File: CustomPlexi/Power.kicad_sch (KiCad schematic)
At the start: 1 part, among them U1 TL074

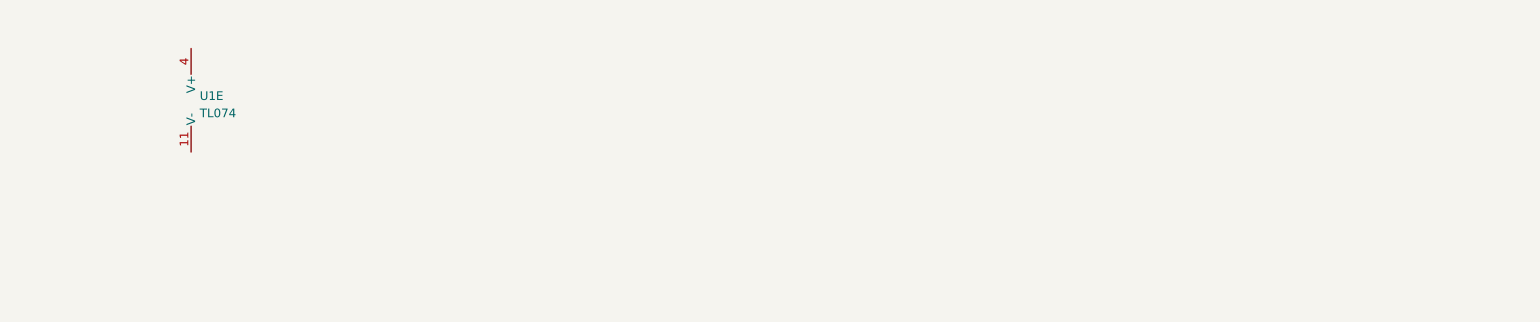
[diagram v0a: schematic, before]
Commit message: input dcdc and negative voltage converter. To decide values
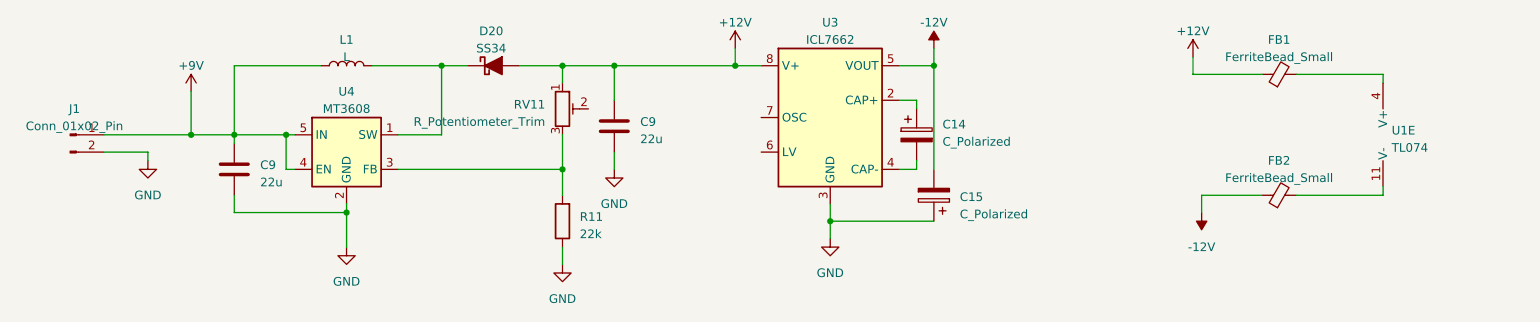
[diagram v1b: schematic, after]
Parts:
- added C14, C15: C_Polarized, symbol Device:C_Polarized
- added C9 (x2): 22u, Capacitor_SMD_AKL:C_0603_1608Metric, symbol PCM_Capacitor_AKL:C_0603
- added D20: SS34, Diode_SMD_AKL:D_SMC, symbol PCM_Diode_Schottky_AKL:SS34
- added FB1, FB2: FerriteBead_Small, symbol Device:FerriteBead_Small
- added J1: Conn_01x02_Pin, symbol Connector:Conn_01x02_Pin
- added L1: L, symbol Device:L
- added R11: 22k, Resistor_SMD_AKL:R_0603_1608Metric, symbol PCM_Resistor_AKL:R_0603
- added RV11: R_Potentiometer_Trim, symbol Device:R_Potentiometer_Trim
- added U3: ICL7662, symbol Regulator_SwitchedCapacitor:ICL7660
- added U4: MT3608, Package_TO_SOT_SMD:SOT-23-6, symbol Regulator_Switching:MT3608
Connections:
- net at U1.11 (V-): now also FB2.2
- net at U1.4 (V+): now also FB1.2
- new net: C14.1, U3.2 (CAP+)
- new net: C14.2, U3.4 (CAP-)
- new net: R11.2, RV11.3, U4.3 (FB)
- new net: D20.1 (K), L1.2, U4.1 (SW)
- new net +12V: C9.2, D20.2 (A), FB1.1, RV11.1, U3.8 (V+)
- new net +9V: C9.2, J1.1 (Pin_1), L1.1, U4.4 (EN), U4.5 (IN)
- new net -12V: C15.2, FB2.1, U3.5 (VOUT)
- new net GND: C15.1, C9.1, C9.1, J1.2 (Pin_2), R11.1, U3.3 (GND), U4.2 (GND)
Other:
- moved on the sheet: U1E

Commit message: commit
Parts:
- C14, C15: footprint (none) -> Capacitor_THT:CP_Radial_D6.3mm_P2.50mm
- C9: footprint Capacitor_SMD_AKL:C_0603_1608Metric -> Capacitor_SMD:C_0402_1005Metric_Pad0.74x0.62mm_HandSolder
- D20: footprint Diode_SMD_AKL:D_SMC -> Diode_SMD:D_0201_0603Metric_Pad0.64x0.40mm_HandSolder
- FB1, FB2: footprint (none) -> PCM_Ferrite_SMD_AKL:Ferrite_0402_1005Metric
- J1: footprint (none) -> Connector_PinHeader_2.54mm:PinHeader_1x02_P2.54mm_Vertical
- L1: footprint (none) -> Inductor_SMD:L_0603_1608Metric
- R11: footprint Resistor_SMD_AKL:R_0603_1608Metric -> Resistor_SMD:R_0402_1005Metric_Pad0.72x0.64mm_HandSolder
- RV11: footprint (none) -> Potentiometer_THT:Potentiometer_Runtron_RM-065_Vertical
- U1: footprint (none) -> Package_SO:SOIC-14W_7.5x9mm_P1.27mm
- U3: footprint (none) -> PCM_Package_SO_AKL:SOIC-8_3.9x4.9mm_P1.27mm
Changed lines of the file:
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@@
       (effects (font (size 1.27 1.27)) (justify right))
     )
-    (property "Footprint" "Capacitor_SMD_AKL:C_0603_1608Metric" (at 52.3748 52.07 0)
+    (property "Footprint" "Capacitor_SMD:C_0402_1005Metric_Pad0.74x0.62mm_HandSolder" (at 52.3748 52.07 0)
       (effects (font (size 1.27 1.27)) hide)
     )
@@
       (effects (font (size 1.27 1.27)) (justify left))
     )
-    (property "Footprint" "" (at 223.52 48.26 0)
+    (property "Footprint" "Package_SO:SOIC-14W_7.5x9mm_P1.27mm" (at 223.52 48.26 0)
       (effects (font (size 1.27 1.27)) hide)
     )
@@
       (effects (font (size 1.27 1.27)))
     )
-    (property "Footprint" "" (at 143.51 50.8 0)
+    (property "Footprint" "PCM_Package_SO_AKL:SOIC-8_3.9x4.9mm_P1.27mm" (at 143.51 50.8 0)
       (effects (font (size 1.27 1.27)) hide)
     )
@@
       (effects (font (size 1.27 1.27)))
     )
-    (property "Footprint" "" (at 207.01 61.468 90)
+    (property "Footprint" "PCM_Ferrite_SMD_AKL:Ferrite_0402_1005Metric" (at 207.01 61.468 90)
       (effects (font (size 1.27 1.27)) hide)
     )
@@
       (effects (font (size 1.27 1.27)) (justify right))
     )
-    (property "Footprint" "Resistor_SMD_AKL:R_0603_1608Metric" (at 101.6 52.07 0)
+    (property "Footprint" "Resistor_SMD:R_0402_1005Metric_Pad0.72x0.64mm_HandSolder" (at 101.6 52.07 0)
       (effects (font (size 1.27 1.27)) hide)
     )
@@
       (effects (font (size 1.27 1.27)))
     )
-    (property "Footprint" "Diode_SMD_AKL:D_SMC" (at 91.44 40.64 0)
+    (property "Footprint" "Diode_SMD:D_0201_0603Metric_Pad0.64x0.40mm_HandSolder" (at 91.44 40.64 0)
       (effects (font (size 1.27 1.27)) hide)
     )
@@
       (effects (font (size 1.27 1.27)) (justify right))
     )
-    (property "Footprint" "Capacitor_SMD_AKL:C_0603_1608Metric" (at 108.2548 45.72 0)
+    (property "Footprint" "Capacitor_SMD:C_0402_1005Metric_Pad0.74x0.62mm_HandSolder" (at 108.2548 45.72 0)
       (effects (font (size 1.27 1.27)) hide)
     )
@@
       (effects (font (size 1.27 1.27)))
     )
-    (property "Footprint" "" (at 29.21 50.8 0)
+    (property "Footprint" "Connector_PinHeader_2.54mm:PinHeader_1x02_P2.54mm_Vertical" (at 29.21 50.8 0)
       (effects (font (size 1.27 1.27)) hide)
     )
@@
       (effects (font (size 1.27 1.27)) (justify right))
     )
-    (property "Footprint" "" (at 101.6 46.99 0)
+    (property "Footprint" "Potentiometer_THT:Potentiometer_Runtron_RM-065_Vertical" (at 101.6 46.99 0)
       (effects (font (size 1.27 1.27)) hide)
     )
@@
       (effects (font (size 1.27 1.27)) (justify left))
     )
-    (property "Footprint" "" (at 154.6352 54.61 0)
+    (property "Footprint" "Capacitor_THT:CP_Radial_D6.3mm_P2.50mm" (at 154.6352 54.61 0)
       (effects (font (size 1.27 1.27)) hide)
     )
@@
       (effects (font (size 1.27 1.27)))
     )
-    (property "Footprint" "" (at 69.85 40.64 0)
+    (property "Footprint" "Inductor_SMD:L_0603_1608Metric" (at 69.85 40.64 0)
       (effects (font (size 1.27 1.27)) hide)
     )
@@
       (effects (font (size 1.27 1.27)))
     )
-    (property "Footprint" "" (at 207.01 43.688 90)
+    (property "Footprint" "PCM_Ferrite_SMD_AKL:Ferrite_0402_1005Metric" (at 207.01 43.688 90)
       (effects (font (size 1.27 1.27)) hide)
     )
@@
       (effects (font (size 1.27 1.27)) (justify right))
     )
-    (property "Footprint" "" (at 155.2448 55.88 0)
-      (effects (font (size 1.27 1.27)) hide)
-    )
+    (property "Footprint" "Capacitor_THT:CP_Radial_D6.3mm_P2.50mm" (at 155.2448 55.88 0)
+      (effects (font (size 1.27 1.27)) hide)
+    )

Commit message: Full ts808
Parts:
- added U5: RC4558, symbol Amplifier_Operational:RC4558
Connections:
- net at FB2.2, U1.11 (V-): now also U5.4 (V-)
- net at FB1.2, U1.4 (V+): now also U5.8 (V+)
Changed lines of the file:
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@@
   (junction (at 60.96 50.8) (diameter 0) (color 0 0 0 0)
   )
+  (junction (at 222.25 59.69) (diameter 0) (color 0 0 0 0)
+  )
   (junction (at 46.99 50.8) (diameter 0) (color 0 0 0 0)
   )
@@
   (junction (at 83.82 40.64) (diameter 0) (color 0 0 0 0)
   )
+  (junction (at 222.25 41.91) (diameter 0) (color 0 0 0 0)
+  )
   (junction (at 156.21 40.64) (diameter 0) (color 0 0 0 0)
   )
@@
     (stroke (width 0) (type default))
   )
+  (wire (pts (xy 233.68 41.91) (xy 222.25 41.91))
+    (stroke (width 0) (type default))
+  )
   (wire (pts (xy 109.22 53.34) (xy 109.22 55.88))
     (stroke (width 0) (type default))
   )
+  (wire (pts (xy 233.68 43.18) (xy 233.68 41.91))
+    (stroke (width 0) (type default))
+  )
   (wire (pts (xy 101.6 55.88) (xy 101.6 59.69))
     (stroke (width 0) (type default))
@@
     (stroke (width 0) (type default))
   )
+  (wire (pts (xy 233.68 59.69) (xy 222.25 59.69))
+    (stroke (width 0) (type default))
+  )
   (wire (pts (xy 222.25 59.69) (xy 222.25 58.42))
     (stroke (width 0) (type default))
@@
   )
   (wire (pts (xy 101.6 67.31) (xy 101.6 69.85))
+    (stroke (width 0) (type default))
+  )
+  (wire (pts (xy 233.68 59.69) (xy 233.68 58.42))
     (stroke (width 0) (type default))
   )
@@
         )
       )
+    )
+  )
+  (symbol (lib_id "Amplifier_Operational:RC4558") (at 236.22 50.8 0) (unit 3)
+    (in_bom yes) (on_board yes) (dnp no) (fields_autoplaced)
+    (property "Reference" "U5" (at 234.95 50.165 0)
+      (effects (font (size 1.27 1.27)) (justify left))
+    )
+    (property "Value" "RC4558" (at 234.95 52.705 0)
+      (effects (font (size 1.27 1.27)) (justify left))
+    )
+    (property "Footprint" "" (at 236.22 50.8 0)
+      (effects (font (size 1.27 1.27)) hide)
+    )
+    (property "Datasheet" "http://www.ti.com/lit/ds/symlink/rc4558.pdf" (at 236.22 50.8 0)
+      (effects (font (size 1.27 1.27)) hide)
+    )
+    (pin "1")
+    (pin "2")
+    (pin "3")
+    (pin "5")
+    (pin "6")
+    (pin "7")
+    (pin "4")
+    (pin "8")
+    (instances
+      (project "CustomPlexi"
+        (path "/cb47f45c-6a2b-402e-a3a9-bf4992e06e45/46194796-04b4-4b0f-a843-2a3656b84ab8"
+          (reference "U5") (unit 3)
+        )
+        (path "/cb47f45c-6a2b-402e-a3a9-bf4992e06e45/c4a7bcdf-70be-4e6d-b7b4-c53de8d52358"
+          (reference "U5") (unit 3)
+        )
+      )

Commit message: changed refdes
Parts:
- renumbered C14 to C18, C15 to C19, D20 to D15, J1 to J3, RV11 to RV10, U4 to U3, U3 to U4
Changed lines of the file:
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@@
   (symbol (lib_id "power:-12V") (at 195.58 62.23 180) (unit 1)
     (in_bom yes) (on_board yes) (dnp no) (fields_autoplaced)
-    (property "Reference" "#PWR025" (at 195.58 64.77 0)
+    (property "Reference" "#PWR024" (at 195.58 64.77 0)
       (effects (font (size 1.27 1.27)) hide)
     )
@@
       (project "CustomPlexi"
         (path "/cb47f45c-6a2b-402e-a3a9-bf4992e06e45/c4a7bcdf-70be-4e6d-b7b4-c53de8d52358"
-          (reference "#PWR025") (unit 1)
+          (reference "#PWR024") (unit 1)
         )
       )
@@
         )
         (path "/cb47f45c-6a2b-402e-a3a9-bf4992e06e45/c4a7bcdf-70be-4e6d-b7b4-c53de8d52358"
-          (reference "#PWR023") (unit 1)
+          (reference "#PWR021") (unit 1)
         )
       )
@@
   (symbol (lib_id "Regulator_SwitchedCapacitor:ICL7660") (at 140.97 48.26 0) (unit 1)
     (in_bom yes) (on_board yes) (dnp no) (fields_autoplaced)
-    (property "Reference" "U3" (at 140.97 34.29 0)
+    (property "Reference" "U4" (at 140.97 34.29 0)
       (effects (font (size 1.27 1.27)))
     )
@@
       (project "CustomPlexi"
         (path "/cb47f45c-6a2b-402e-a3a9-bf4992e06e45/c4a7bcdf-70be-4e6d-b7b4-c53de8d52358"
-          (reference "U3") (unit 1)
+          (reference "U4") (unit 1)
         )
       )
@@
   (symbol (lib_id "power:+12V") (at 127 38.1 0) (unit 1)
     (in_bom yes) (on_board yes) (dnp no) (fields_autoplaced)
-    (property "Reference" "#PWR021" (at 127 41.91 0)
+    (property "Reference" "#PWR020" (at 127 41.91 0)
       (effects (font (size 1.27 1.27)) hide)
     )
@@
       (project "CustomPlexi"
         (path "/cb47f45c-6a2b-402e-a3a9-bf4992e06e45/c4a7bcdf-70be-4e6d-b7b4-c53de8d52358"
-          (reference "#PWR021") (unit 1)
+          (reference "#PWR020") (unit 1)
         )
       )
@@
         )
         (path "/cb47f45c-6a2b-402e-a3a9-bf4992e06e45/c4a7bcdf-70be-4e6d-b7b4-c53de8d52358"
-          (reference "#PWR026") (unit 1)
+          (reference "#PWR017") (unit 1)
         )
       )
@@
         )
         (path "/cb47f45c-6a2b-402e-a3a9-bf4992e06e45/c4a7bcdf-70be-4e6d-b7b4-c53de8d52358"
-          (reference "#PWR019") (unit 1)
+          (reference "#PWR015") (unit 1)
         )
       )
@@
   (symbol (lib_id "power:+9V") (at 46.99 44.45 0) (unit 1)
     (in_bom yes) (on_board yes) (dnp no) (fields_autoplaced)
-    (property "Reference" "#PWR020" (at 46.99 48.26 0)
+    (property "Reference" "#PWR016" (at 46.99 48.26 0)
       (effects (font (size 1.27 1.27)) hide)
     )
@@
       (project "CustomPlexi"
         (path "/cb47f45c-6a2b-402e-a3a9-bf4992e06e45/c4a7bcdf-70be-4e6d-b7b4-c53de8d52358"
-          (reference "#PWR020") (unit 1)
+          (reference "#PWR016") (unit 1)
         )
       )
@@
         )
         (path "/cb47f45c-6a2b-402e-a3a9-bf4992e06e45/c4a7bcdf-70be-4e6d-b7b4-c53de8d52358"
-          (reference "R19") (unit 1)
+          (reference "R18") (unit 1)
         )
       )
@@
   (symbol (lib_id "PCM_Diode_Schottky_AKL:SS34") (at 91.44 40.64 180) (unit 1)
     (in_bom yes) (on_board yes) (dnp no) (fields_autoplaced)
-    (property "Reference" "D20" (at 91.1225 35.56 0)
+    (property "Reference" "D15" (at 91.1225 35.56 0)
       (effects (font (size 1.27 1.27)))
     )
@@
       (project "CustomPlexi"
         (path "/cb47f45c-6a2b-402e-a3a9-bf4992e06e45/c4a7bcdf-70be-4e6d-b7b4-c53de8d52358"
-          (reference "D20") (unit 1)
+          (reference "D15") (unit 1)
         )
       )
@@
         )
         (path "/cb47f45c-6a2b-402e-a3a9-bf4992e06e45/c4a7bcdf-70be-4e6d-b7b4-c53de8d52358"
-          (reference "U5") (unit 3)
+          (reference "U2") (unit 3)
         )
       )
@@
   (symbol (lib_id "power:+12V") (at 194.31 39.37 0) (unit 1)
     (in_bom yes) (on_board yes) (dnp no) (fields_autoplaced)
-    (property "Reference" "#PWR024" (at 194.31 43.18 0)
+    (property "Reference" "#PWR023" (at 194.31 43.18 0)
       (effects (font (size 1.27 1.27)) hide)
     )
@@
       (project "CustomPlexi"
         (path "/cb47f45c-6a2b-402e-a3a9-bf4992e06e45/c4a7bcdf-70be-4e6d-b7b4-c53de8d52358"
-          (reference "#PWR024") (unit 1)
+          (reference "#PWR023") (unit 1)
         )
       )
@@
   (symbol (lib_id "Connector:Conn_01x02_Pin") (at 29.21 50.8 0) (unit 1)
     (in_bom yes) (on_board yes) (dnp no) (fields_autoplaced)
-    (property "Reference" "J1" (at 29.845 46.99 0)
+    (property "Reference" "J3" (at 29.845 46.99 0)
       (effects (font (size 1.27 1.27)))
     )
@@
       (project "CustomPlexi"
         (path "/cb47f45c-6a2b-402e-a3a9-bf4992e06e45/c4a7bcdf-70be-4e6d-b7b4-c53de8d52358"
-          (reference "J1") (unit 1)
+          (reference "J3") (unit 1)
         )
       )
@@
   (symbol (lib_id "Device:R_Potentiometer_Trim") (at 101.6 46.99 0) (unit 1)
     (in_bom yes) (on_board yes) (dnp no) (fields_autoplaced)
-    (property "Reference" "RV11" (at 99.06 46.355 0)
+    (property "Reference" "RV10" (at 99.06 46.355 0)
       (effects (font (size 1.27 1.27)) (justify right))
     )
@@
       (project "CustomPlexi"
         (path "/cb47f45c-6a2b-402e-a3a9-bf4992e06e45/c4a7bcdf-70be-4e6d-b7b4-c53de8d52358"
-          (reference "RV11") (unit 1)
+          (reference "RV10") (unit 1)
         )
       )
@@
   (symbol (lib_id "Device:C_Polarized") (at 153.67 50.8 0) (unit 1)
     (in_bom yes) (on_board yes) (dnp no) (fields_autoplaced)
-    (property "Reference" "C14" (at 157.48 49.276 0)
+    (property "Reference" "C18" (at 157.48 49.276 0)
       (effects (font (size 1.27 1.27)) (justify left))
     )
@@
       (project "CustomPlexi"
         (path "/cb47f45c-6a2b-402e-a3a9-bf4992e06e45/c4a7bcdf-70be-4e6d-b7b4-c53de8d52358"
-          (reference "C14") (unit 1)
+          (reference "C18") (unit 1)
         )
       )
@@
         )
         (path "/cb47f45c-6a2b-402e-a3a9-bf4992e06e45/c4a7bcdf-70be-4e6d-b7b4-c53de8d52358"
-          (reference "#PWR028") (unit 1)
+          (reference "#PWR019") (unit 1)
         )
       )
@@
   (symbol (lib_id "Regulator_Switching:MT3608") (at 69.85 53.34 0) (unit 1)
     (in_bom yes) (on_board yes) (dnp no) (fields_autoplaced)
-    (property "Reference" "U4" (at 69.85 44.45 0)
+    (property "Reference" "U3" (at 69.85 44.45 0)
       (effects (font (size 1.27 1.27)))
     )
@@
       (project "CustomPlexi"
         (path "/cb47f45c-6a2b-402e-a3a9-bf4992e06e45/c4a7bcdf-70be-4e6d-b7b4-c53de8d52358"
-          (reference "U4") (unit 1)
+          (reference "U3") (unit 1)
         )
       )
@@
   (symbol (lib_id "Device:C_Polarized") (at 156.21 59.69 180) (unit 1)
     (in_bom yes) (on_board yes) (dnp no) (fields_autoplaced)
-    (property "Reference" "C15" (at 160.02 59.944 0)
+    (property "Reference" "C19" (at 160.02 59.944 0)
       (effects (font (size 1.27 1.27)) (justify right))
     )
@@
       (project "CustomPlexi"
         (path "/cb47f45c-6a2b-402e-a3a9-bf4992e06e45/c4a7bcdf-70be-4e6d-b7b4-c53de8d52358"
-          (reference "C15") (unit 1)
+          (reference "C19") (unit 1)
         )
       )
@@
         )
         (path "/cb47f45c-6a2b-402e-a3a9-bf4992e06e45/c4a7bcdf-70be-4e6d-b7b4-c53de8d52358"
-          (reference "#PWR027") (unit 1)
-        )
-      )
+          (reference "#PWR018") (unit 1)
+        )
+      )
